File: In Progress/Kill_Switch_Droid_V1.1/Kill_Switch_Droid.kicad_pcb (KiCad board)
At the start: 4 copper layers, 88 x 36 mm, 54 parts, among them J1 USB_B_Micro, J2 Power In, J3 U.FL-R-SMT-1(10), J4 External Switch In, J5 Output, Q2 UMH3N, Q3 BSS138, U1 ESP32-PICO-MINI-02, U2 CP2102N-A02-GQFN28, U3 LP5912-3.3DRV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

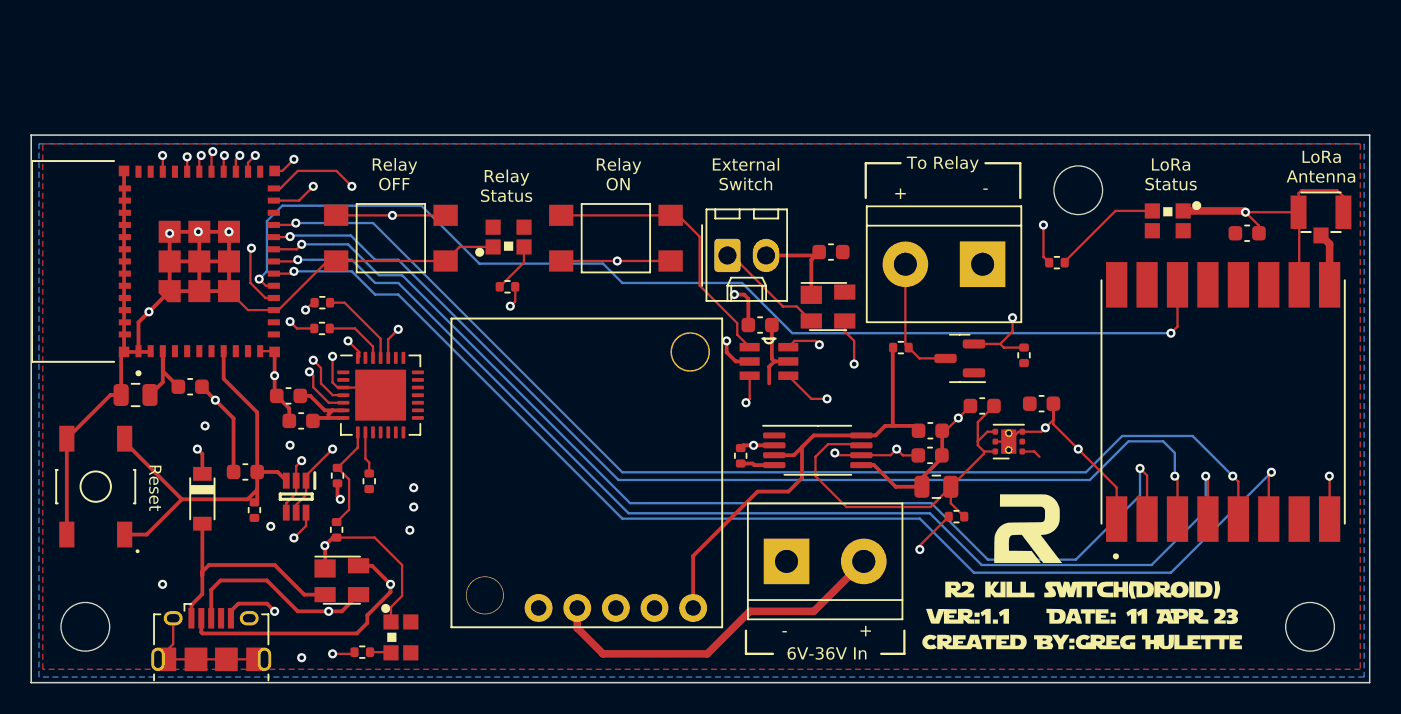
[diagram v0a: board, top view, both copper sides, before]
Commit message: Updating the Kill Switch Droid side
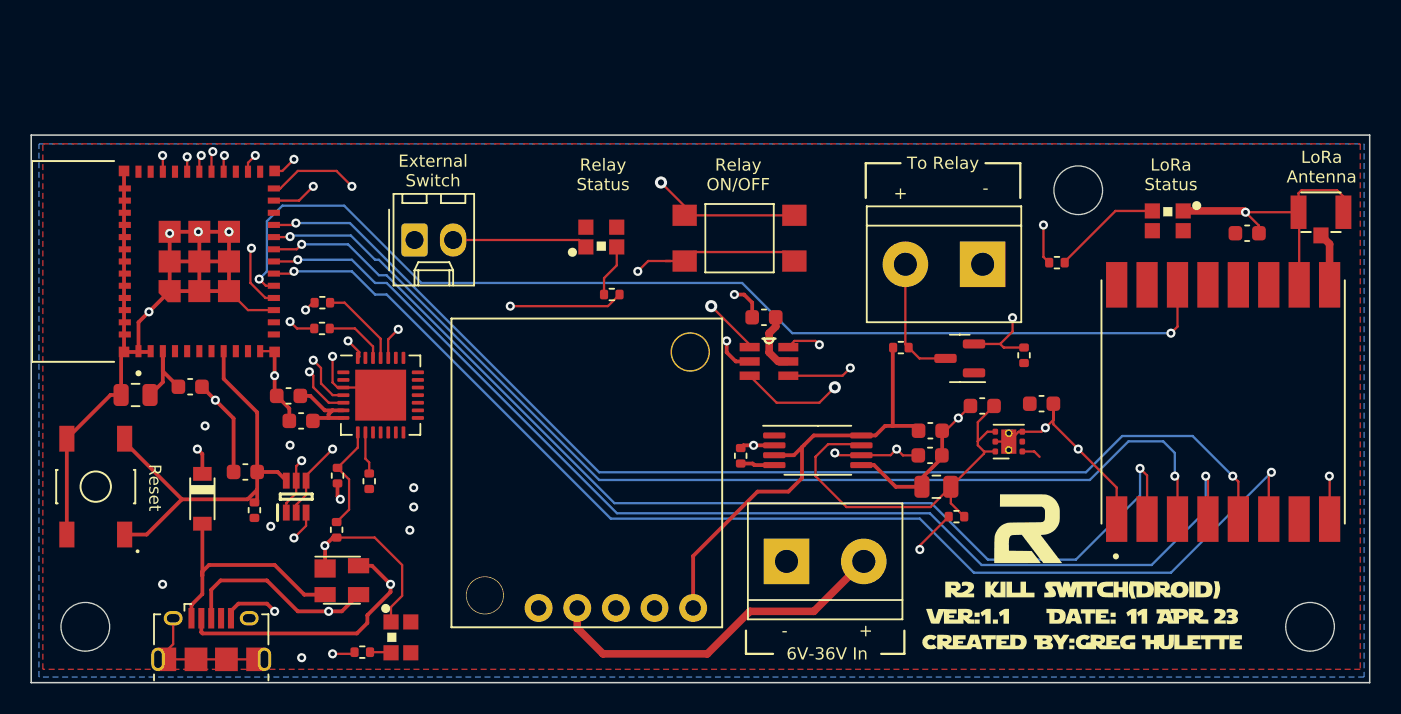
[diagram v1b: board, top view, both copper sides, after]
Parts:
- removed C13: .1uF, Capacitor_SMD:C_0603_1608Metric
- removed S3: TL3305CF260QG, Custom:TL3305CF260QG
- removed U8: MAX6816, Package_TO_SOT_SMD:SOT-143
- moved J4 20.6 mm to (57.2, 58.9)
- moved S2 8.13 mm to (78.6, 58.8)
- moved R17 6.88 mm to (70.2, 62.5)
- moved L3 6.10 mm to (69.5, 58.7)
- moved C11 0.57 mm to (80.2, 64.0)
- turned Q2 to 90 degrees
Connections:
- J4 pad 1: Net-(J4-Pad1) -> Net-(U6-Pad3)
- Q2 pad 1: DTR -> RTS
- Q2 pad 2: RTS -> DTR
- Q2 pad 3: RESET -> GPIO0
- Q2 pad 4: RTS -> DTR
- Q2 pad 5: DTR -> RTS
- Q2 pad 6: GPIO0 -> RESET
- U1 pad 27: OFF_SW_OUT -> unconnected-(U1-Pad27)
- U6 pad 3: Net-(S3-Pad1) -> Net-(U6-Pad3)
- U6 pad 4: OFF_SW_OUT -> EXT_SW_OUT
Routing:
- net OFF_SW_OUT: track 58.4 -> 0.00 mm, vias 2 -> 0
- net Net-(U6-Pad3): track 0.00 -> 42.6 mm, vias 0 -> 1
- net Net-(S3-Pad1): track 37.4 -> 0.00 mm, vias 2 -> 0
- net GND: track 182.9 -> 172.8 mm
- net Net-(J4-Pad1): track 7.30 -> 0.00 mm
- net RELAY_LED_DATA: track 27.9 -> 35.0 mm
- net Net-(S2-Pad1): track 18.3 -> 23.2 mm, vias 0 -> 2
- net EXT_SW_OUT: track 50.5 -> 52.2 mm
- net +3V3: track 79.5 -> 78.6 mm
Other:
- board text added: "Relay ON/OFF"
- board text removed: "Relay OFF"
- board text removed: "Relay ON"

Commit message: some minor updates
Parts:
- removed the G*** at (101.1, 83.6)
- added G***: LOGO, Logos:R2DroidGateway, F.Cu at (102.1, 84.1)
- added J6: Conn_01x03, Connector_Molex:Molex_KK-254_AE-6410-03A_1x03_P2.54mm_Vertical, F.Cu at (53.6, 58.9)
- C10, C11, C12, C2, C3, C5, C9: footprint Capacitor_SMD:C_0603_1608Metric -> Capacitor_SMD:C_0402_1005Metric
- C4: footprint Capacitor_SMD:C_0603_1608Metric -> Capacitor_SMD:C_0805_2012Metric
- J3: value U.FL-R-SMT-1(10) -> 73391-0083; footprint Custom:HRS_U.FL-R-SMT-1(10) -> Custom:73391-0083
- moved J4 6.35 mm to (63.6, 58.9)
- moved J3 4.58 mm to (115.1, 52.8), turned to -90 degrees
- moved C10 3.66 mm to (108.9, 60.5)
- moved U5 1.78 mm to (110.4, 71.3)
- moved L3 1.52 mm to (71.0, 58.7)
- moved C4 0.25 mm to (49.7, 71.0)
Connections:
- J3 pad 2: Net-(J3-Pad2) -> GND
- U1 pad 22: unconnected-(U1-Pad22) -> TX_HEADER
- U1 pad 27: unconnected-(U1-Pad27) -> RX_HEADER
- U5 pad 9: Net-(J3-Pad2) -> Net-(J3-Pad5)
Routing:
- net RX_HEADER: track 0.00 -> 16.9 mm
- net TX_HEADER: track 0.00 -> 9.96 mm
- net Net-(J4-Pad1): track 42.6 -> 34.0 mm
- net Net-(J3-Pad5): track 0.00 -> 7.78 mm
- net GND: track 172.8 -> 166.6 mm
- net Net-(J3-Pad2): track 3.48 -> 0.00 mm
- net EXT_SW_OUT: track 52.2 -> 55.0 mm
- net NSS_LORA: track 74.9 -> 76.7 mm
- net SCK_LORA: track 76.3 -> 78.0 mm
- net MOSI_LORA: track 71.7 -> 73.5 mm
- net RESET_LORA: track 79.7 -> 81.5 mm
- net MISO_LORA: track 72.7 -> 74.5 mm
- net Net-(L3-Pad3): track 3.47 -> 4.29 mm
- net DI0_LORA: track 71.9 -> 71.1 mm
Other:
- board text added: "G"
- board text added: "Rx"
- board text added: "Serial"
- board text added: "Tx"
- board text removed: "LoRa Antenna"
